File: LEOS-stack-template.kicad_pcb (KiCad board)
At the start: 2 copper layers, 100 x 100 mm, 35 parts, among them J1 MicroFit_1x4, J2 MicroFit_1x4, U1 MCP2562FD, U2 MCP2518FD, U3 TPS55287, U4 MPM3620A, Y1 40 MHz

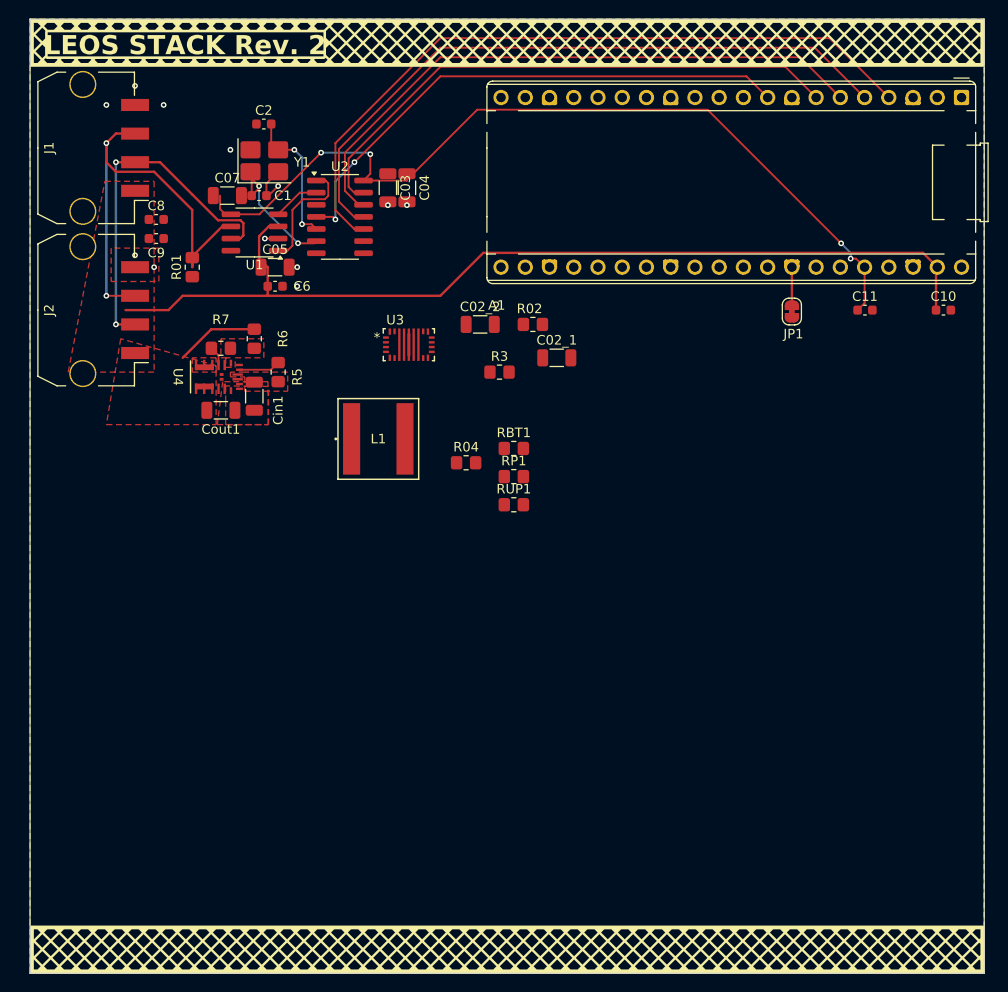
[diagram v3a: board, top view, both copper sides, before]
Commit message: mostly routed the vin to 12V buck converter
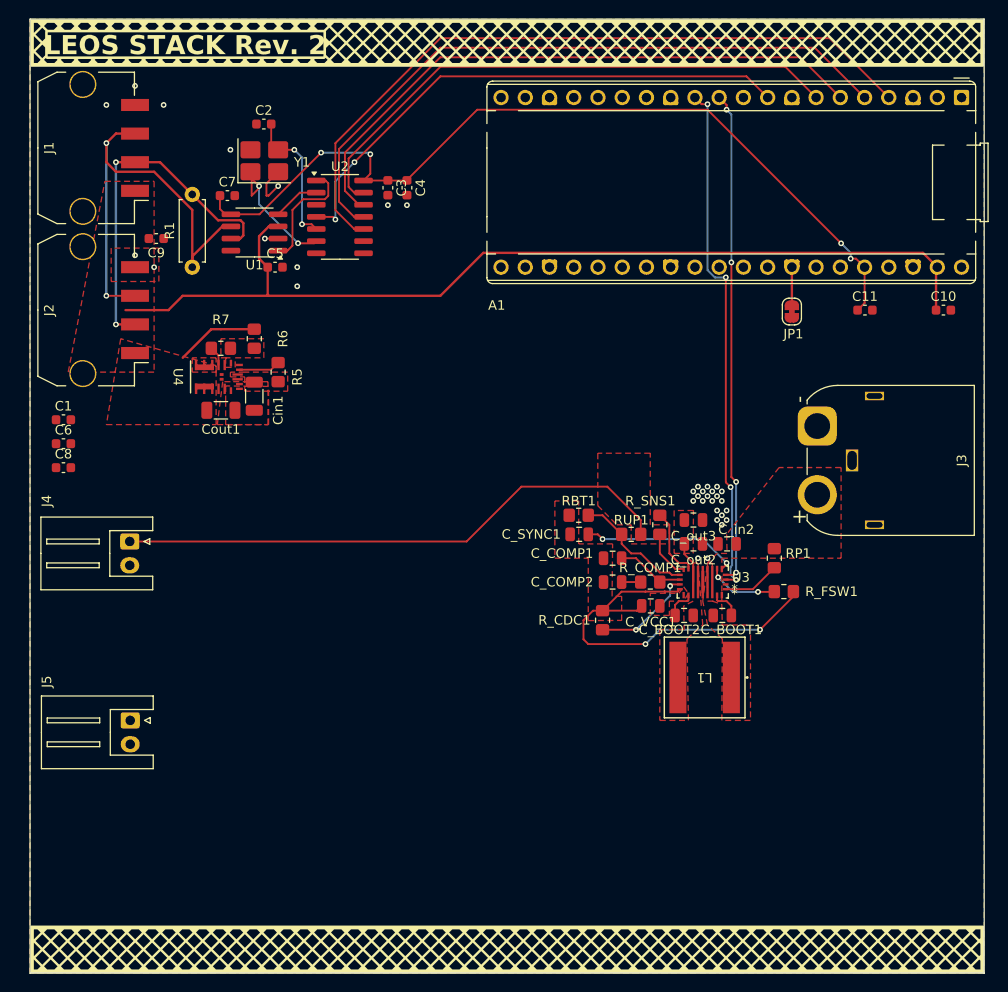
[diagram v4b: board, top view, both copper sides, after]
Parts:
- added C1: 12pF, Capacitor_SMD:C_0603_1608Metric, F.Cu at (103.5, 92.0)
- added C6: 1uF, Capacitor_SMD:C_0603_1608Metric, F.Cu at (103.5, 94.5)
- added C8: 47uF, Capacitor_SMD:C_0603_1608Metric, F.Cu at (103.5, 97.0)
- added C_BOOT1: 0.1uF, Capacitor_SMD:C_0805_2012Metric, F.Cu at (172.6, 112.5)
- added C_BOOT2: 0.1uF, Capacitor_SMD:C_0805_2012Metric, F.Cu at (168.6, 112.5)
- added C_COMP1: 36.5nF, Capacitor_SMD:C_0805_2012Metric, F.Cu at (161.1, 106.5)
- added C_VCC1: 4.7uF, Capacitor_SMD:C_0805_2012Metric, F.Cu at (165.1, 111.5)
- added J3: Conn_01x02_MountingPin, Connector_AMASS:AMASS_XT60IPW-M_1x03_P7.20mm_Horizontal, F.Cu at (182.5, 92.7)
- added J4: Conn_01x02_Socket, Connector_JST:JST_XH_S2B-XH-A_1x02_P2.50mm_Horizontal, F.Cu at (110.4, 104.8)
- added J5: Conn_01x02_Socket, Connector_JST:JST_XH_S2B-XH-A_1x02_P2.50mm_Horizontal, F.Cu at (110.5, 123.5)
- added R_FSW1: 9.3k, Resistor_SMD:R_0805_2012Metric_Pad1.20x1.40mm_HandSolder, F.Cu at (179.0, 110.0)
- C3: renamed from C03; value 4.7uF -> 0.1uF; footprint Capacitor_SMD:C_1206_3216Metric -> Capacitor_SMD:C_0603_1608Metric
- C4: renamed from C04; value 0.1uF -> 1uF; footprint Capacitor_SMD:C_1206_3216Metric -> Capacitor_SMD:C_0603_1608Metric
- C5: renamed from C05; footprint Capacitor_SMD:C_1206_3216Metric -> Capacitor_SMD:C_0603_1608Metric
- C7: renamed from C07; value 36.5nF -> 0.1uF; footprint Capacitor_SMD:C_1206_3216Metric -> Capacitor_SMD:C_0603_1608Metric
- C_COMP2: renamed from C6; value 1uF -> 18.2nF; footprint Capacitor_SMD:C_0603_1608Metric -> Capacitor_SMD:C_0805_2012Metric
- C_SYNC1: renamed from C8; value 47uF -> 47nF; footprint Capacitor_SMD:C_0603_1608Metric -> Capacitor_SMD:C_0805_2012Metric
- C_in2: renamed from C1; value 12pF -> 47uF; footprint Capacitor_SMD:C_0603_1608Metric -> Capacitor_SMD:C_0805_2012Metric
- C_out2: renamed from C02_1; footprint Capacitor_SMD:C_1206_3216Metric -> Capacitor_SMD:C_0805_2012Metric
- C_out3: renamed from C02_2; footprint Capacitor_SMD:C_1206_3216Metric -> Capacitor_SMD:C_0805_2012Metric
- R1: renamed from R01; value 9.3k -> 120R; footprint Resistor_SMD:R_0805_2012Metric_Pad1.20x1.40mm_HandSolder -> Resistor_THT:R_Axial_DIN0207_L6.3mm_D2.5mm_P7.62mm_Horizontal
- moved C_in2 61.1 mm to (173.1, 105.0), turned to 180 degrees
- moved C_SYNC1 55.3 mm to (157.6, 104.0), turned to 180 degrees
- moved C_COMP2 47.0 mm to (161.1, 109.0), turned to 180 degrees
- moved L1 42.4 mm to (170.7, 119.0), turned to 180 degrees
- moved U3 39.6 mm to (170.5, 109.0), turned to 180 degrees
- moved R_CDC1 31.8 mm to (160.0, 113.0), turned to 90 degrees
- moved C_out3 30.3 mm to (169.5, 102.5), turned to 180 degrees
- moved RP1 28.6 mm to (178.0, 106.5), turned to -90 degrees
- moved R_COMP1 27.1 mm to (165.0, 109.0), turned to 180 degrees
- moved C_out2 24.2 mm to (169.5, 105.0), turned to 180 degrees
- moved R_SNS1 21.3 mm to (166.0, 103.0), turned to -90 degrees
- moved RUP1 12.7 mm to (163.0, 104.0)
- moved RBT1 9.76 mm to (157.5, 102.0)
- renumbered R02 to R_CDC1, R3 to R_COMP1, R04 to R_SNS1
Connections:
- C3 pad 1: Net-(U3-VCC) -> VDD
- C3 pad 2: GNDA -> GND
- C4 pad 1: Net-(U3-SW1) -> VDD
- C4 pad 2: Net-(U3-BOOT1) -> GND
- C5 pad 1: Net-(U3-SW2) -> +5V
- C5 pad 2: Net-(U3-BOOT2) -> GND
- C7 pad 1: Net-(U3-COMP) -> VDD
- C7 pad 2: Net-(C06-Pad2) -> GND
- C_COMP2 pad 1: +5V -> Net-(C_COMP2-Pad1)
- C_COMP2 pad 2: GND -> GNDA
- C_SYNC1 pad 1: +5V -> Net-(U3-DITH/SYNC)
- C_SYNC1 pad 2: GND -> GNDA
- C_in2 pad 1: /OSC1 -> VDC
- R1 pad 1: Net-(U3-FSW) -> /CAN-
- R1 pad 2: GNDA -> /CAN+
- R_COMP1 pad 2: Net-(C06-Pad1) -> Net-(C_COMP2-Pad1)
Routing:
- net +12V: track 0.00 -> 64.1 mm
- net I2C0_SCL: track 0.00 -> 54.7 mm, vias 0 -> 4
- net I2C0_SDA: track 0.00 -> 51.7 mm, vias 0 -> 4
- net GNDA: track 0.00 -> 42.6 mm, vias 0 -> 2
- net Net-(U3-DITH/SYNC): track 0.00 -> 16.6 mm, vias 0 -> 2
- net Net-(U3-FB/INT): track 0.00 -> 12.8 mm
- net Net-(U3-ISP): track 0.00 -> 11.7 mm
- net Net-(U3-CDC): track 0.00 -> 10.7 mm, vias 0 -> 2
- net Net-(U3-FSW): track 0.00 -> 7.49 mm, vias 0 -> 2
- net Net-(U3-COMP): track 0.00 -> 7.24 mm
- net Net-(U3-EN/UVLO): track 0.00 -> 6.03 mm
- net Net-(U3-BOOT1): track 0.00 -> 3.25 mm
- net Net-(U3-BOOT2): track 0.00 -> 3.21 mm
- net Net-(C_COMP2-Pad1): track 0.00 -> 2.00 mm
- net GND: vias 12 -> 34
- added copper zone on F.Cu, net +12V
- added copper zone on F.Cu, net GNDA
- added copper zone on F.Cu, net Net-(U3-ISP)
- added copper zone on F.Cu, net Net-(U3-SW1)
- added copper zone on F.Cu, net Net-(U3-SW2)
- added copper zone on F.Cu, net Net-(U3-VCC)
- added copper zone on F.Cu, net VDC

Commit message: added some more ground nodes
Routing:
- net GND: vias 34 -> 41
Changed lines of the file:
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@@
+	)
+	(via
+		(at 162 113.25)
+		(size 0.6)
+		(drill 0.3)
+		(layers "F.Cu" "B.Cu")
+		(free yes)
+		(net 13)
 	)
 	(via
@@
 	)
 	(via
+		(at 162.25 112.75)
+		(size 0.6)
+		(drill 0.3)
+		(layers "F.Cu" "B.Cu")
+		(free yes)
+		(net 13)
+	)
+	(via
+		(at 163 112.75)
+		(size 0.6)
+		(drill 0.3)
+		(layers "F.Cu" "B.Cu")
+		(free yes)
+		(net 13)
+	)
+	(via
 		(at 172 100)
 		(size 0.6)
@@
 	)
 	(via
+		(at 162.75 113.25)
+		(size 0.6)
+		(drill 0.3)
+		(layers "F.Cu" "B.Cu")
+		(free yes)
+		(net 13)
+	)
+	(via
 		(at 172 101.5)
 		(size 0.6)
@@
 	)
 	(via
+		(at 162.25 110.75)
+		(size 0.6)
+		(drill 0.3)
+		(layers "F.Cu" "B.Cu")
+		(free yes)
+		(net 13)
+	)
+	(via
 		(at 170.5 99.5)
 		(size 0.6)
@@
 	)
 	(via
+		(at 163.75 112.75)
+		(size 0.6)
+		(drill 0.3)
+		(layers "F.Cu" "B.Cu")
+		(free yes)
+		(net 13)
+	)
+	(via
 		(at 171.5 99.5)
 		(size 0.6)
@@
 	(via
 		(at 137.5 69.5)
+		(size 0.6)
+		(drill 0.3)
+		(layers "F.Cu" "B.Cu")
+		(free yes)
+		(net 13)
+	)
+	(via
+		(at 163 110.75)
 		(size 0.6)
 		(drill 0.3)
@@
 		(polygon
 			(pts
-				(xy 155 100.5) (xy 155 106.5) (xy 158.5 106.5) (xy 158.5 113.041667) (xy 162 113.019231) (xy 162 110.5)
+				(xy 155 100.5) (xy 155 106.5) (xy 158.5 106.5) (xy 158.5 113.041667) (xy 161.75 113.020834) (xy 161.75 110.5)
 				(xy 161 110.5) (xy 161.05 105) (xy 157.5 105) (xy 157.5 100.5)
 			)

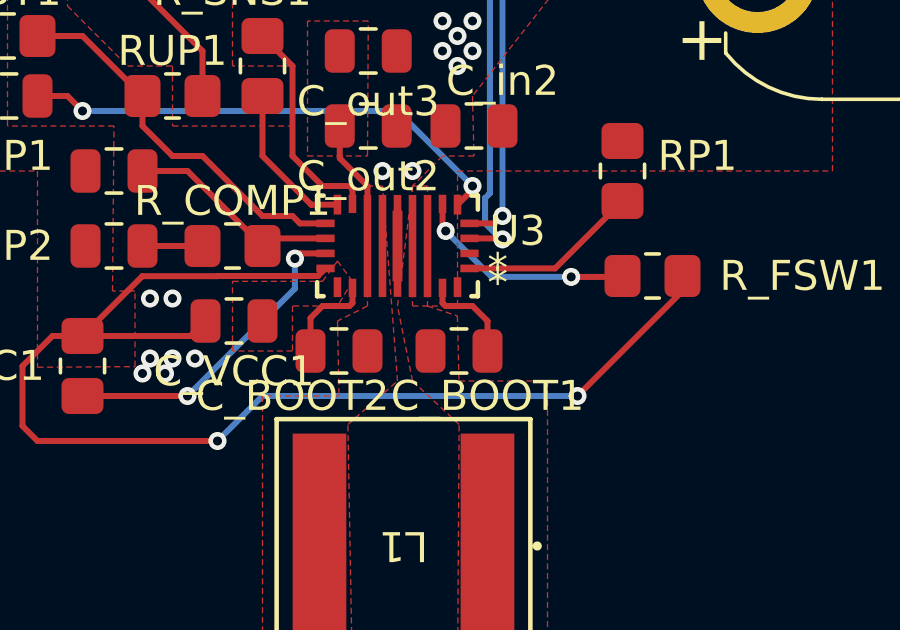
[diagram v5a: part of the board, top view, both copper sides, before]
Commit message: connected the Vin to 12V buck converter to ground!!!!!!
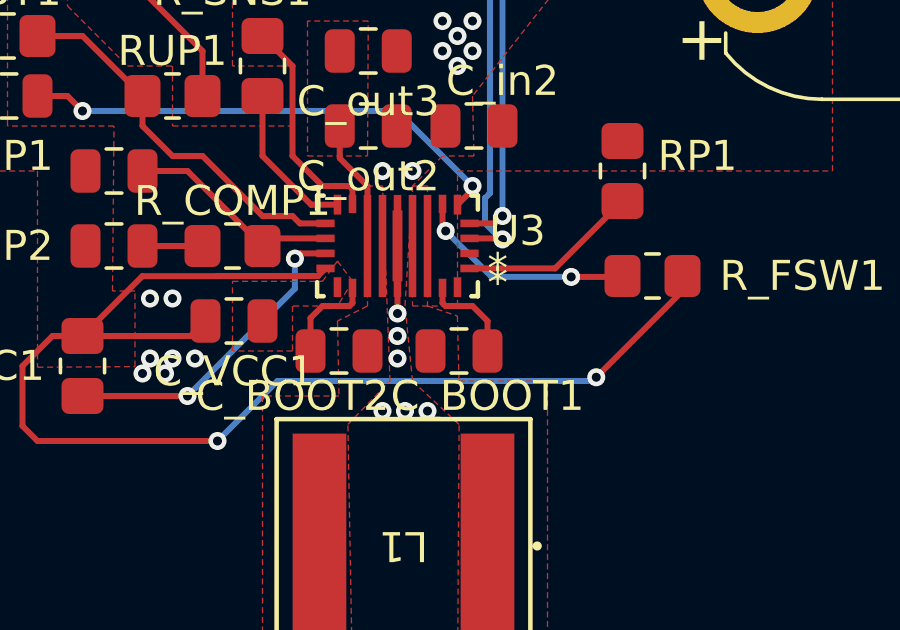
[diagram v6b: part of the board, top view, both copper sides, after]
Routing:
- net GND: track 6.54 -> 8.45 mm, vias 41 -> 47
